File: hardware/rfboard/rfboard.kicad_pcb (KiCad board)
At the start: 2 copper layers, 21 x 44 mm, 20 parts, among them J1 10118194-0001LF, P2 CONN_01X03, P3 CONN_01X04, U1 SAMD21E18, U2 RFM69CW-915MHZ, U3 MIC5504-3.3YM5-T5, U4 74LVC1G125

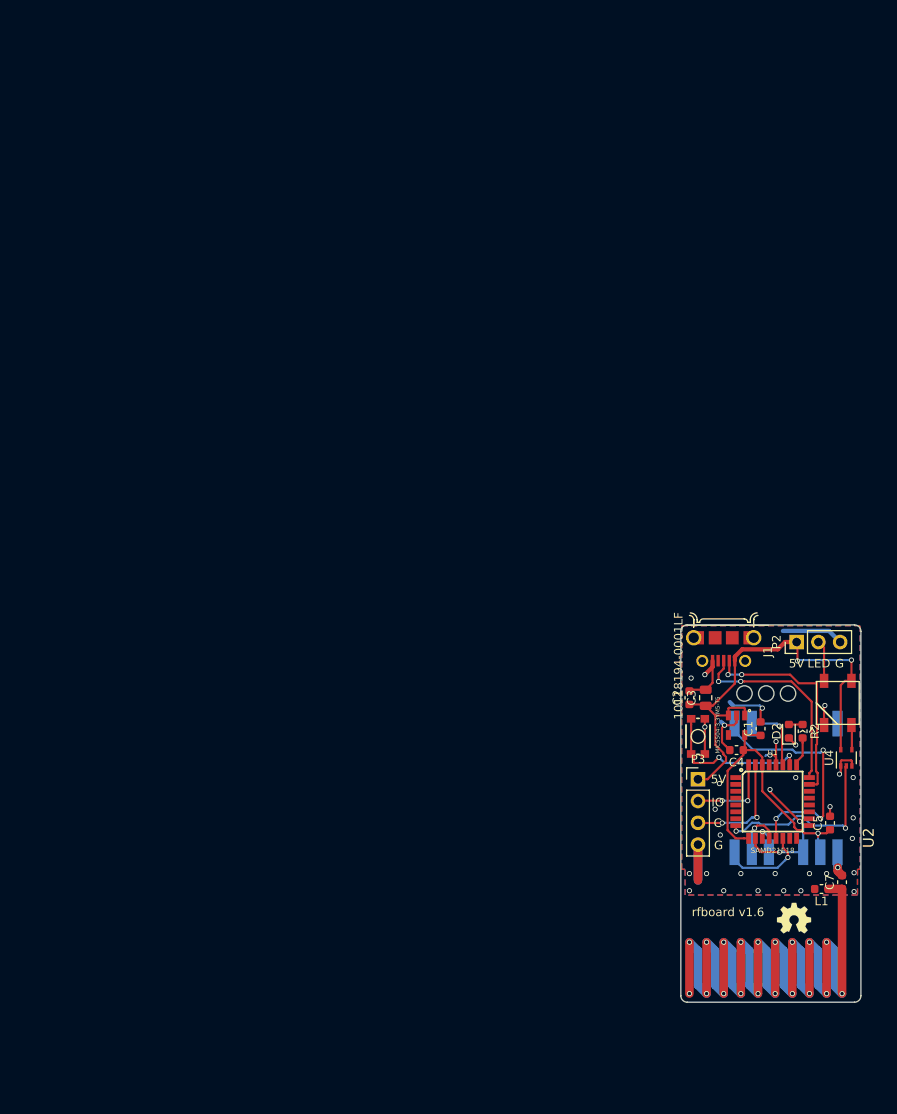
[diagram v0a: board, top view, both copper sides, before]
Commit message: rfboard: add LC filter for radio
Change-Id: I23dd460225624ee06ec1c7d5b5e8e44295342c63
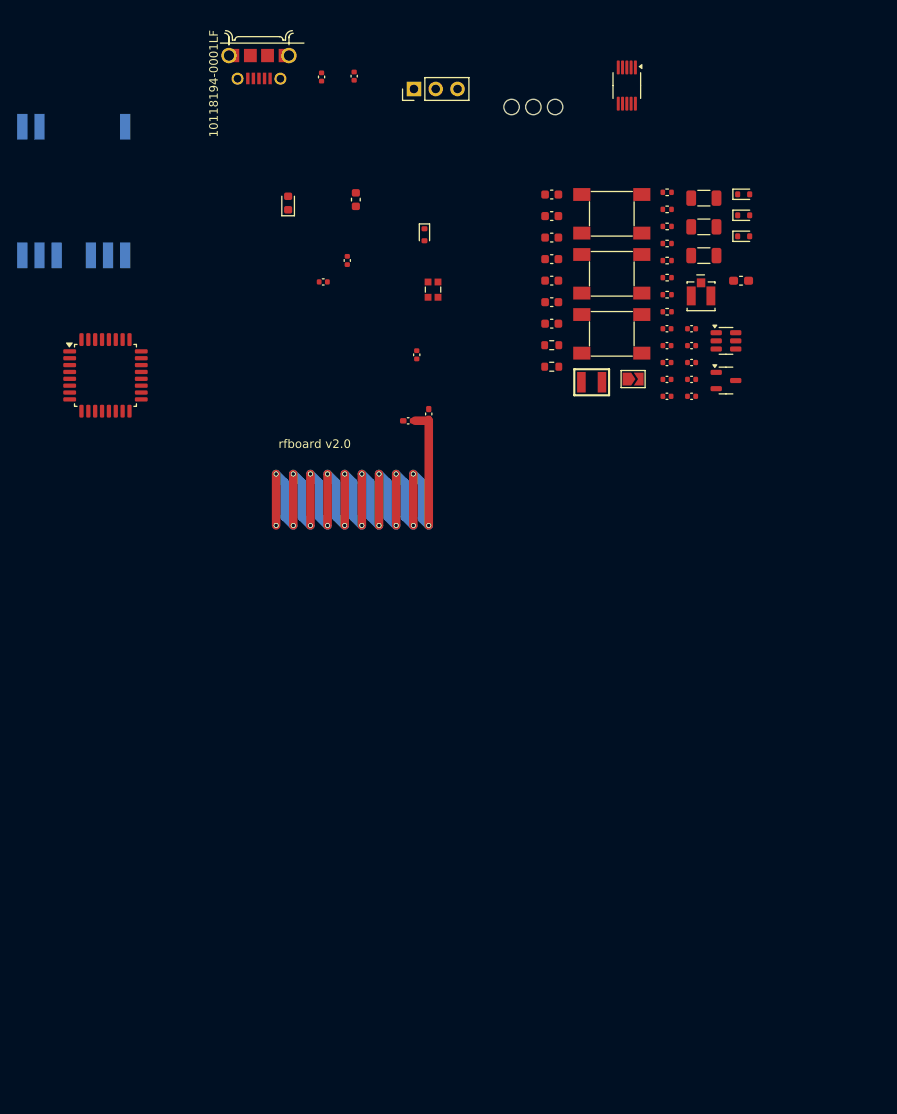
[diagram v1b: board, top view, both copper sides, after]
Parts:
- removed G***: OSHW_LOGO_4mm, homebrew:OSHW_LOGO_4mm
- removed P3: CONN_01X04, Connector_PinHeader_2.54mm:PinHeader_1x04_P2.54mm_Vertical
- removed S1: MOMENTARY-SWITCH-SPST-SMD-4.6X2.8MM, Sparkfun-Switches:TACTILE_SWITCH_SMD_4.6X2.8MM
- added C10: 47uF, Capacitor_SMD:C_1206_3216Metric, F.Cu at (103.7, 43.2)
- added C11: 100nF, Capacitor_SMD:C_0402_1005Metric, F.Cu at (99.4, 60.4)
- added C12: 10uF, Capacitor_SMD:C_0603_1608Metric, F.Cu at (85.9, 47.8)
- added C13: 100nF, Capacitor_SMD:C_0402_1005Metric, F.Cu at (99.4, 62.4)
- added C14: 10uF, Capacitor_SMD:C_0603_1608Metric, F.Cu at (85.9, 50.3)
- added C15: 47uF, Capacitor_SMD:C_1206_3216Metric, F.Cu at (103.7, 46.6)
- added C16: 100nF, Capacitor_SMD:C_0402_1005Metric, F.Cu at (99.4, 64.4)
- added C17: 10uF, Capacitor_SMD:C_0603_1608Metric, F.Cu at (85.9, 52.9)
- added C18: 100nF, Capacitor_SMD:C_0402_1005Metric, F.Cu at (99.4, 66.3)
- added C19: 47uF, Capacitor_SMD:C_1206_3216Metric, F.Cu at (103.7, 49.9)
- added C20: 10uF, Capacitor_SMD:C_0603_1608Metric, F.Cu at (85.9, 55.4)
- added C21: 100nF, Capacitor_SMD:C_0402_1005Metric, F.Cu at (102.3, 58.5)
- added C22: 100nF, Capacitor_SMD:C_0402_1005Metric, F.Cu at (102.3, 60.4)
- added C23: 100nF, Capacitor_SMD:C_0402_1005Metric, F.Cu at (102.3, 62.4)
- added C24: 47pF, Capacitor_SMD:C_0402_1005Metric, F.Cu at (102.3, 64.4)
- added C25: 100nF, Capacitor_SMD:C_0402_1005Metric, F.Cu at (102.3, 66.3)
- added C26: 10uF, Capacitor_SMD:C_0603_1608Metric, F.Cu at (85.9, 57.9)
- added C6: 10uF, Capacitor_SMD:C_0603_1608Metric, F.Cu at (85.9, 42.8)
- added C8: 100nF, Capacitor_SMD:C_0402_1005Metric, F.Cu at (99.4, 58.5)
- added C9: 10uF, Capacitor_SMD:C_0603_1608Metric, F.Cu at (85.9, 45.3)
- added D3: SRV05-4-P-T7, Package_TO_SOT_SMD:SOT-23-6, F.Cu at (106.3, 59.9)
- added D4: ESD5Z5.0, Diode_SMD:D_SOD-523, F.Cu at (108.3, 42.8)
- added D5: ESD5Z5.0, Diode_SMD:D_SOD-523, F.Cu at (108.3, 45.2)
- added D6: ESD5Z5.0, Diode_SMD:D_SOD-523, F.Cu at (108.3, 47.7)
- added FB1: FerriteBead, Inductor_SMD:L_0603_1608Metric_Pad1.05x0.95mm_HandSolder, F.Cu at (108.0, 52.9)
- added J3: 2337019-1, Homebrew:CONN_2337019-1, F.Cu at (103.4, 54.7)
- added JP1: SolderJumper_2_Open, Jumper:SolderJumper-2_P1.3mm_Open_TrianglePad1.0x1.5mm, F.Cu at (95.4, 64.3)
- added R1: 4k7, Resistor_SMD:R_0402_1005Metric, F.Cu at (99.4, 42.5)
- added R10: 10k, Resistor_SMD:R_0402_1005Metric, F.Cu at (99.4, 54.5)
- added R11: 15k, Resistor_SMD:R_0402_1005Metric, F.Cu at (99.4, 56.5)
- added R3: 22k, Resistor_SMD:R_0402_1005Metric, F.Cu at (99.4, 44.5)
- added R4: 1k, Resistor_SMD:R_0402_1005Metric, F.Cu at (99.4, 46.5)
- added R5: 470, Resistor_SMD:R_0402_1005Metric, F.Cu at (99.4, 48.5)
- added R6: 470, Resistor_SMD:R_0402_1005Metric, F.Cu at (99.4, 50.5)
- added R7: 1k, Resistor_SMD:R_0603_1608Metric, F.Cu at (85.9, 60.4)
- added R8: 1k, Resistor_SMD:R_0603_1608Metric, F.Cu at (85.9, 62.9)
- added R9: 10k, Resistor_SMD:R_0402_1005Metric, F.Cu at (99.4, 52.5)
- added SW1: SW_Push, Homebrew:SW_TACTILE_5.1MM_TS-1187A-C-D-B, F.Cu at (92.9, 45.1)
- added SW2: SW_Push, Homebrew:SW_TACTILE_5.1MM_TS-1187A-C-D-B, F.Cu at (92.9, 52.1)
- added SW3: SW_Push, Homebrew:SW_TACTILE_5.1MM_TS-1187A-C-D-B, F.Cu at (92.9, 59.1)
- added U5: XC6206P332MR-G, Package_TO_SOT_SMD:SOT-23-3, F.Cu at (106.3, 64.5)
- added U6: HX 1210-C06, easyeda2kicad:SMD-2P_L2.9-W2.4_C9900033648, F.Cu at (90.6, 64.7)
- C1, C2, C4, C5: value 1uF -> 100nF; footprint Capacitor_SMD:C_0603_1608Metric -> Capacitor_SMD:C_0402_1005Metric
- C3: value 10uF -> 100nF; footprint Capacitor_SMD:C_0805_2012Metric -> Capacitor_SMD:C_0402_1005Metric
- C7: footprint Capacitor_SMD:C_0603_1608Metric -> Capacitor_SMD:C_0402_1005Metric_Pad0.74x0.62mm_HandSolder
- D1: value WS2812B -> ESD5Z5.0; footprint homebrew:WS2812B -> Diode_SMD:D_SOD-523
- D2: value LED -> RED
- L1: footprint Inductor_SMD:L_0603_1608Metric -> Inductor_SMD:L_0402_1005Metric_Pad0.77x0.64mm_HandSolder
- U1: value SAMD21E18 -> STM32G070KBTx; footprint Sparkfun-Silicon-Standard:TQFP32-08 -> Package_QFP:LQFP-32_7x7mm_P0.8mm
- U3: value MIC5504-3.3YM5-T5 -> CH340X; footprint MIC5504-3.3YM5-T5:SOT23-5P95_280X145XL45X37N -> Package_SO:MSOP-10_3x3mm_P0.5mm
- U4: value 74LVC1G125 -> XL-0807RGBC-WS2812B; footprint Package_TO_SOT_SMD:SOT-353_SC-70-5 -> easyeda2kicad:LED-SMD_4P-L2.0-W1.8_CY-0807
- moved U2 108.4 mm to (30.2, 42.4)
- moved U1 92.3 mm to (33.9, 63.9)
- moved J1 86.9 mm to (51.8, 26.6)
- moved D2 84.9 mm to (55.2, 43.8)
- moved C2 84.1 mm to (59.1, 29.1)
- moved C3 83.3 mm to (62.9, 29.0)
- moved R2 81.0 mm to (63.1, 43.4)
- moved P2 78.4 mm to (69.9, 30.5)
- moved U3 75.7 mm to (94.7, 30.1)
- moved H3 73.6 mm to (83.8, 32.6)
- moved C4 72.8 mm to (59.3, 53.0)
- moved C5 72.8 mm to (70.2, 61.5)
- moved C7 72.8 mm to (71.6, 68.4)
- moved D1 72.8 mm to (71.1, 47.5)
- moved L1 72.8 mm to (69.2, 69.2)
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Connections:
- net ANTENNA renamed /ANTENNA
- C1 pad 1: +3V3 -> +5V
- C2 pad 1: +5V -> Net-(U3-V3)
- C5 pad 1: +3V3 -> Net-(U2-3.3V)
- C7 pad 2: Net-(C6-Pad2) -> Net-(JP1-A)
- D1 pad 1: +5V -> /SW1
- D1 pad 2: LED_EXTERNAL -> GND
- D2 pad 2: Net-(D2-Pad2) -> Net-(D2-A)
- P2 pad 2: LED_EXTERNAL -> /LED_EXTERNAL
- R2 pad 1: Net-(D2-Pad2) -> /SIMPLE_LED
- R2 pad 2: SIMPLE_LED -> Net-(D2-A)
- U1 pad 1: (no net) -> unconnected-(U1-PB9-Pad1)
- U1 pad 10: GND -> /VIBRATION_SENSOR
- U1 pad 11: RADIO_MOSI -> /LED_INTERNAL
- U1 pad 12: RADIO_SCK -> unconnected-(U1-PA5-Pad12)
- U1 pad 13: RADIO_MISO -> unconnected-(U1-PA6-Pad13)
- U1 pad 14: RADIO_NSS -> unconnected-(U1-PA7-Pad14)
- U1 pad 15: (no net) -> unconnected-(U1-PB0-Pad15)
- U1 pad 16: (no net) -> /SIMPLE_LED
- U1 pad 17: (no net) -> unconnected-(U1-PB2-Pad17)
- U1 pad 18: (no net) -> unconnected-(U1-PA8-Pad18)
- U1 pad 19: (no net) -> unconnected-(U1-NC/PA9-Pad19)
- U1 pad 2: (no net) -> unconnected-(U1-PC14-Pad2)
- U1 pad 20: (no net) -> unconnected-(U1-PC6-Pad20)
- U1 pad 21: (no net) -> unconnected-(U1-NC/PA10-Pad21)
- U1 pad 22: (no net) -> /USART_TX
- U1 pad 23: USB_D- -> /USART_RX
- U1 pad 24: USB_D+ -> /SWDIO
- U1 pad 25: SIMPLE_LED -> /BOOT0
- U1 pad 26: RESET_SW -> /RADIO_NSS
- U1 pad 27: RADIO_DIO0 -> /RADIO_SCK
- U1 pad 28: GND -> /RADIO_MISO
- U1 pad 29: (no net) -> /RADIO_MOSI
- U1 pad 3: (no net) -> unconnected-(U1-PC15-Pad3)
- U1 pad 30: +3V3 -> /SW1
- U1 pad 31: ARM_SWCLK -> /SW2
- U1 pad 32: ARM_SWDIO -> unconnected-(U1-PB8-Pad32)
- U1 pad 4: (no net) -> +3V3
- U1 pad 5: (no net) -> GND
- U1 pad 6: (no net) -> Net-(D6-K)
- U1 pad 7: (no net) -> /5V_DIVIDED
- U1 pad 8: LED_INTERNAL -> unconnected-(U1-PA1-Pad8)
- U1 pad 9: +3V3 -> /RADIO_DIO0
- U3 pad 1: +5V -> /USB_DP
- U3 pad 2: GND -> /USB_DN
- U3 pad 3: +5V -> GND
- U3 pad 4: (no net) -> /~{RTS}
- U3 pad 5: +3V3 -> unconnected-(U3-~{CTS}-Pad5)
- U4 pad 1: GND -> +5V
- U4 pad 2: LED_INTERNAL -> Net-(U4-DOUT)
- U4 pad 4: Net-(D1-Pad4) -> Net-(U4-DIN)
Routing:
- net GND: track 68.5 -> 0.00 mm, vias 34 -> 0
- net +5V: track 54.1 -> 0.00 mm, vias 2 -> 0
- net +3V3: track 36.3 -> 0.00 mm, vias 1 -> 0
- net RADIO_MISO: track 28.6 -> 0.00 mm, vias 3 -> 0
- net USB_D-: track 25.3 -> 0.00 mm, vias 2 -> 0
- net USB_D+: track 23.5 -> 0.00 mm, vias 2 -> 0
- net LED_INTERNAL: track 22.2 -> 0.00 mm, vias 2 -> 0
- net RESET_SW: track 18.4 -> 0.00 mm, vias 2 -> 0
- net ARM_SWCLK: track 13.4 -> 0.00 mm, vias 2 -> 0
- net RADIO_NSS: track 10.5 -> 0.00 mm, vias 1 -> 0
- net ARM_SWDIO: track 10.1 -> 0.00 mm, vias 2 -> 0
- net RADIO_DIO0: track 8.02 -> 0.00 mm, vias 1 -> 0
- net RADIO_SCK: track 5.91 -> 0.00 mm, vias 1 -> 0
- net LED_EXTERNAL: track 4.80 -> 0.00 mm
- net Net-(C6-Pad2): track 3.82 -> 0.00 mm, vias 1 -> 0
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- removed copper zone on B.Cu, net GND
- removed copper zone on F.Cu, net GND
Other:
- board outline removed
- board text added: "rfboard v2.0"
- board text removed: "5V"
- board text removed: "C"
- board text removed: "G"
- board text removed: "GND"
- board text removed: "I"
- board text removed: "IO"
- board text removed: "LED"
- board text removed: "REG"
- board text removed: "rfboard v1.6"

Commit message: rfboard: first pass at component placement for v2.0
Change-Id: I4c465cc58b982850d15f3562f19207050c8a0873
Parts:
- added J2: Conn_01x04, Homebrew:PinHeader_1x04_P2.54mm_Vertical_NoPlastic, F.Cu at (61.5, 118.1)
- H3: footprint homebrew:3_pin_2.54mm_pitch_strain_relief -> Homebrew:3_pin_2.54mm_pitch_strain_relief
- J1: footprint homebrew:FRAMATOME_10118194-0001LF_fixed_bridges -> Homebrew:FRAMATOME_10118194-0001LF_fixed_bridges
- R2, R7, R8: footprint Resistor_SMD:R_0603_1608Metric -> Resistor_SMD:R_0402_1005Metric
- U2: value RFM69CW-915MHZ -> RFM69HCW; footprint homebrew:RFM69CW-minimalpads -> Homebrew:RFM69HCW-minimalpads
- U4: footprint easyeda2kicad:LED-SMD_4P-L2.0-W1.8_CY-0807 -> Homebrew:LED-SMD_4P-L2.0-W1.8_CY-0807
- U6: footprint easyeda2kicad:SMD-2P_L2.9-W2.4_C9900033648 -> Homebrew:SMD-2P_L2.9-W2.4_C9900033648
- moved U2 90.0 mm to (71.1, 122.6), turned to -90 degrees
- moved FB1 87.2 mm to (67.7, 130.2)
- moved J3 84.5 mm to (72.3, 133.3), turned to -90 degrees
- moved D5 80.3 mm to (70.0, 115.7), turned to 180 degrees
- moved C6 79.5 mm to (79.1, 122.0), turned to 90 degrees
- moved R9 78.6 mm to (65.0, 123.1), turned to 180 degrees
- moved C2 76.9 mm to (75.6, 104.2), turned to 180 degrees
- moved C20 76.5 mm to (70.9, 130.4)
- moved D4 75.9 mm to (65.7, 105.5), turned to 180 degrees
- moved D6 75.1 mm to (76.7, 115.7), turned to 180 degrees
- moved D2 74.5 mm to (65.1, 117.6), turned to 0 degrees
- moved R2 74.4 mm to (67.6, 117.6), turned to 180 degrees
- moved C26 73.0 mm to (68.1, 128.7)
- moved C3 72.9 mm to (78.7, 100.2), turned to 0 degrees
- moved C4 71.5 mm to (77.9, 122.0), turned to 90 degrees
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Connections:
- J1 pad 2: USB_D- -> /USB_DN
- J1 pad 3: USB_D+ -> /USB_DP
- J1 pad 4: (no net) -> unconnected-(J1-ID-Pad4)
- U2 pad 1: Net-(C6-Pad2) -> GND
- U2 pad 14: GND -> /RADIO_DIO0
- U2 pad 2: +3V3 -> /RADIO_MISO
- U2 pad 3: GND -> /RADIO_MOSI
- U2 pad 5: RADIO_MOSI -> /RADIO_NSS
- U2 pad 8: RADIO_MISO -> GND
- U2 pad 9: RADIO_DIO0 -> Net-(JP1-A)
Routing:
- net Net-(U2-3.3V): track 0.00 -> 9.15 mm, vias 0 -> 2
- net GND: track 0.00 -> 8.55 mm, vias 0 -> 4
- net /USB_DP: track 0.00 -> 7.99 mm, vias 0 -> 2
- net /USB_DN: track 0.00 -> 6.75 mm, vias 0 -> 3
- net Net-(JP1-A): track 0.00 -> 5.86 mm, vias 0 -> 2
- net /ANTENNA_UFL: track 0.00 -> 1.86 mm
- net +3V3: track 0.00 -> 1.71 mm
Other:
- board outline added: 20 x 59 mm
- copper layers 2 -> 4
- rule pad_to_mask_clearance: 0.2 -> 0

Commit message: rfboard PCB v2.0
Change-Id: Ic39936a14b05c72f947b18cbfe92ca4c5239ed35
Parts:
- added D7: ESD5Z5.0, Diode_SMD:D_SOD-523, F.Cu at (65.3, 96.4)
- added J4: Conn_01x02, Homebrew:PinHeader_1x02_P2.54mm_Vertical_NoPlastic, F.Cu at (70.1, 95.4)
- moved C8 9.16 mm to (72.3, 97.2), turned to -90 degrees
- moved C1 5.33 mm to (72.3, 99.1), turned to 90 degrees
- moved C10 4.73 mm to (72.8, 104.2), turned to -90 degrees
- moved R3 3.50 mm to (75.6, 103.9)
- moved R1 2.10 mm to (74.5, 103.3), turned to -90 degrees
- moved C2 1.88 mm to (76.0, 102.4), turned to 0 degrees
- moved L1 0.83 mm to (77.2, 134.7)
- moved J3 0.30 mm to (72.6, 133.3)
- moved JP1 0.26 mm to (76.7, 132.9)
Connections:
- D3 pad 4: /LED_EXTERNAL -> unconnected-(D3-IO3-Pad4)
- U1 pad 10: /VIBRATION_SENSOR -> unconnected-(U1-PA3-Pad10)
- U1 pad 18: unconnected-(U1-PA8-Pad18) -> /VIBRATION_SENSOR
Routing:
- net GND: track 8.55 -> 122.5 mm, vias 4 -> 73
- net +3V3: track 1.71 -> 77.4 mm, vias 0 -> 7
- net +5V: track 0.00 -> 67.3 mm, vias 0 -> 6
- net /BOOT0: track 0.00 -> 36.0 mm, vias 0 -> 2
- net /SW1: track 0.00 -> 32.8 mm, vias 0 -> 5
- net Net-(D6-K): track 0.00 -> 31.7 mm, vias 0 -> 7
- net /USART_TX: track 0.00 -> 30.9 mm, vias 0 -> 2
- net /USART_RX: track 0.00 -> 30.5 mm, vias 0 -> 2
- net /5V_DIVIDED: track 0.00 -> 30.1 mm, vias 0 -> 4
- net /SW2: track 0.00 -> 24.6 mm, vias 0 -> 4
- net /LED_INTERNAL: track 0.00 -> 21.7 mm, vias 0 -> 4
- net /RADIO_DIO0: track 0.00 -> 19.2 mm, vias 0 -> 1
- net /RADIO_MISO: track 0.00 -> 15.5 mm, vias 0 -> 3
- net /RADIO_MOSI: track 0.00 -> 14.5 mm, vias 0 -> 1
- net /RADIO_NSS: track 0.00 -> 13.1 mm, vias 0 -> 1
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- added copper zone on B.Cu, net GND
- added copper zone on F.Cu, net GND
- added copper zone on In1.Cu, net GND
- added copper zone on In2.Cu, net GND
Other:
- outline, holes or cut-outs redrawn
- board text added: "3V3"
- board text added: "5"
- board text added: "5V"
- board text added: "ANT"
- board text added: "CLK"
- board text added: "D"
- board text added: "DATA"
- board text added: "G"
- board text added: "GND"
- board text added: "IO"
- board text added: "RST"
